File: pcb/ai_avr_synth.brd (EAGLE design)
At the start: 99.1 x 69.8 mm, 49 parts, among them IC1 ATMEGA328P-PDIP, J1 1X02ST, J2 1X06, J3 1X08, J4 1X08, J5 MIDIJACK, U1 MC7805, U2 TLC2262, U3 6N138

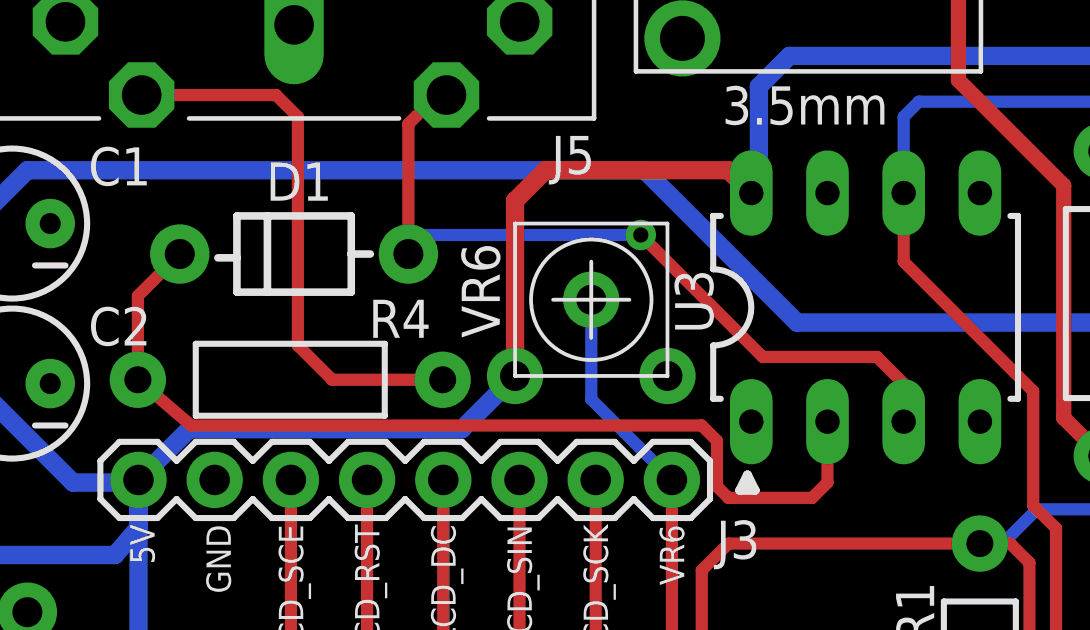
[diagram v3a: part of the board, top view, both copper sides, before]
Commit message: fixed trimmer footprint
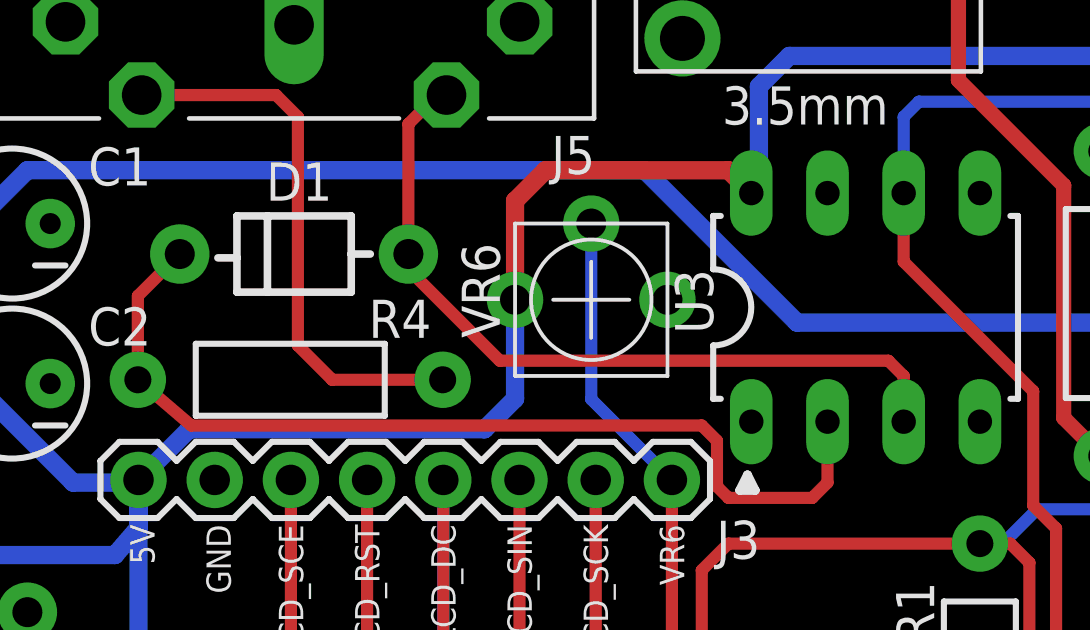
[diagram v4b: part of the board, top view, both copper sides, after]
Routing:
- net LCD_LED: track 47.1 -> 49.7 mm
- net N$10: track 26.1 -> 26.0 mm, vias 1 -> 0
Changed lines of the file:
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@@
 <wire x1="49.53" y1="57.404" x2="48.26" y2="56.134" width="0.6096" layer="1"/>
 <wire x1="13.61" y1="42" x2="15.298" y2="43.688" width="0.6096" layer="16"/>
-<wire x1="15.298" y1="43.688" x2="24.384" y2="43.688" width="0.6096" layer="16"/>
-<wire x1="24.384" y1="43.688" x2="26.162" y2="45.466" width="0.6096" layer="16"/>
-<wire x1="26.162" y1="45.466" x2="26.162" y2="51.308" width="0.6096" layer="1"/>
+<wire x1="15.298" y1="43.688" x2="25.146" y2="43.688" width="0.6096" layer="16"/>
+<wire x1="26.162" y1="48.006" x2="26.162" y2="51.308" width="0.6096" layer="1"/>
 <wire x1="26.162" y1="51.308" x2="27.178" y2="52.324" width="0.6096" layer="1"/>
 <wire x1="27.178" y1="52.324" x2="33.274" y2="52.324" width="0.6096" layer="1"/>
@@
 <wire x1="34.29" y1="55.118" x2="35.306" y2="56.134" width="0.6096" layer="16"/>
 <wire x1="35.306" y1="56.134" x2="48.26" y2="56.134" width="0.6096" layer="16"/>
+<wire x1="26.162" y1="48.006" x2="26.162" y2="44.704" width="0.6096" layer="16"/>
+<wire x1="26.162" y1="44.704" x2="25.146" y2="43.688" width="0.6096" layer="16"/>
 </signal>
 <signal name="RESET">
@@
 <wire x1="31.39" y1="2" x2="31.39" y2="42" width="0.4064" layer="1"/>
 <contactref element="VR6" pad="2"/>
-<wire x1="28.702" y1="48.006" x2="28.702" y2="44.688" width="0.4064" layer="16"/>
+<wire x1="28.702" y1="50.546" x2="28.702" y2="44.688" width="0.4064" layer="16"/>
 <wire x1="28.702" y1="44.688" x2="31.39" y2="42" width="0.4064" layer="16"/>
 </signal>
@@
 <contactref element="D1" pad="A"/>
 <contactref element="U3" pad="3"/>
-<wire x1="22.606" y1="49.53" x2="23.241" y2="50.165" width="0.4064" layer="16"/>
-<wire x1="23.241" y1="50.165" x2="30.353" y2="50.165" width="0.4064" layer="16"/>
-<via x="30.353" y="50.165" extent="1-16" drill="0.508"/>
-<wire x1="30.353" y1="50.165" x2="34.417" y2="46.101" width="0.4064" layer="1"/>
-<wire x1="34.417" y1="46.101" x2="38.227" y2="46.101" width="0.4064" layer="1"/>
-<wire x1="38.227" y1="46.101" x2="39.116" y2="45.212" width="0.4064" layer="1"/>
-<wire x1="39.116" y1="45.212" x2="39.116" y2="43.942" width="0.4064" layer="1"/>
 <wire x1="22.606" y1="49.53" x2="22.606" y2="53.866" width="0.4064" layer="1"/>
 <contactref element="J5" pad="5"/>
 <wire x1="23.876" y1="54.83" x2="23.57" y2="54.83" width="0.4064" layer="1"/>
 <wire x1="23.57" y1="54.83" x2="22.606" y2="53.866" width="0.4064" layer="1"/>
+<wire x1="22.606" y1="49.53" x2="22.606" y2="49.022" width="0.4064" layer="1"/>
+<wire x1="22.606" y1="49.022" x2="25.654" y2="45.974" width="0.4064" layer="1"/>
+<wire x1="25.654" y1="45.974" x2="38.608" y2="45.974" width="0.4064" layer="1"/>
+<wire x1="38.608" y1="45.974" x2="39.116" y2="45.466" width="0.4064" layer="1"/>
+<wire x1="39.116" y1="45.466" x2="39.116" y2="43.942" width="0.4064" layer="1"/>
 </signal>
 <signal name="N$12">

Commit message: updating
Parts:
- D1: value (none) -> 1N4148
- D2: value (none) -> 1N4001
- IC1: device Ai_IC:DIL28-3 -> Ai_IC:DIL28
- STANDOFF5, STANDOFF6, STANDOFF7, STANDOFF8: value STAND-OFF -> STAND-OFF4; device Ai_Electromechanical:STAND-OFF -> Ai_Electromechanical:STAND-OFF-4
- U$5: value AI-LOGOL -> AI-LOGOXS; device Ai_Miscellany:AI-LOGO-L -> Ai_Miscellany:AI-LOGO-XS
- U1: value MC7805 -> MC7805-HOR
- U2, U3: device Ai_IC:DIL08-3 -> Ai_IC:DIL08
- XL1: device Ai_FrequencyControl:CRYSTAL-HC49S -> Ai_FrequencyControl:HC49S
- moved VR6 2.50 mm to (28.1, 50.4), turned to 270 degrees
- moved VR1 1.50 mm to (52.3, 34.0)
- moved R4 1.14 mm to (18.7, 46.5)
- moved U$5 1.08 mm to (65.5, 61.3)
- moved S8 1.02 mm to (2.29, 50.9)
- moved J3 1.00 mm to (22.5, 43.0)
- moved J4 1.00 mm to (22.5, 3.00)
- moved VR2 1.00 mm to (65.8, 34.0)
- moved C1 0.80 mm to (9.14, 51.3)
- moved C2 0.80 mm to (9.14, 46.0)
- moved D1 0.76 mm to (18.8, 50.3)
- moved VR3 0.50 mm to (79.2, 34.0)
- moved J1 0.38 mm to (3.68, 60.5)
- renumbered J2 to FTDI
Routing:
- net 9V: track 66.1 -> 73.5 mm
- net 5V: track 269.9 -> 272.0 mm
- net N$10: track 26.0 -> 28.1 mm
- net LCD_LED: track 49.7 -> 47.7 mm
- net N$1: track 18.4 -> 17.3 mm
- net LCD_DC: track 116.5 -> 117.5 mm
- net TXO: track 59.7 -> 60.6 mm
- net N$9: track 32.5 -> 33.3 mm
- net SEMIS: track 21.7 -> 22.4 mm
- net LCD_SCK: track 77.9 -> 77.2 mm
- net CENTS: track 18.6 -> 18.0 mm
- net N$5: track 17.4 -> 16.8 mm
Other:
- outline, holes or cut-outs redrawn
- board text added: "ACROBOTIC Synth Kit"
- board text added: "http://acrobotic.com/synth-kit"
- board text added: "v1.3"
- board text removed: "Ai AVR SYNTHESIZER"
- board text removed: "Design by: Sam Stratter (humanHardDrive)"
- board text removed: "http://acrobotic.com/avr-synthesizer"
- board text removed: "v1.2"

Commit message: adding additional licensing information
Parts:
- added FRAME1: FRAME-LETTER, Ai_Miscellany:CREATIVE-COMMONS
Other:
- board text added: "@MakerBro"
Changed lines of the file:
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@@
 <?xml version="1.0" encoding="utf-8"?>
 <!DOCTYPE eagle SYSTEM "eagle.dtd">
-<eagle version="6.5.0">
+<eagle version="7.1.0">
 <drawing>
 <settings>
@@
 <setting verticaltext="up"/>
 </settings>
-<grid distance="5" unitdist="mil" unit="mil" style="lines" multiple="1" display="yes" altdistance="0.025" altunitdist="inch" altunit="inch"/>
+<grid distance="50" unitdist="mil" unit="mil" style="lines" multiple="1" display="yes" altdistance="0.025" altunitdist="inch" altunit="inch"/>
 <layers>
 <layer number="1" name="Top" color="4" fill="1" visible="yes" active="yes"/>
@@
 <layer number="20" name="Dimension" color="15" fill="1" visible="yes" active="yes"/>
 <layer number="21" name="tPlace" color="7" fill="1" visible="yes" active="yes"/>
-<layer number="22" name="bPlace" color="7" fill="1" visible="yes" active="yes"/>
+<layer number="22" name="bPlace" color="13" fill="1" visible="yes" active="yes"/>
 <layer number="23" name="tOrigins" color="15" fill="1" visible="yes" active="yes"/>
 <layer number="24" name="bOrigins" color="15" fill="1" visible="yes" active="yes"/>
@@
 <layer number="49" name="Reference" color="7" fill="1" visible="yes" active="yes"/>
 <layer number="50" name="dxf" color="7" fill="1" visible="no" active="no"/>
-<layer number="51" name="tDocu" color="7" fill="1" visible="no" active="yes"/>
+<layer number="51" name="tDocu" color="14" fill="1" visible="yes" active="yes"/>
 <layer number="52" name="bDocu" color="7" fill="1" visible="no" active="yes"/>
 <layer number="53" name="tGND_GNDA" color="7" fill="9" visible="no" active="no"/>
@@
 <layer number="59" name="tCarbon" color="7" fill="1" visible="no" active="no"/>
 <layer number="60" name="bCarbon" color="7" fill="1" visible="no" active="no"/>
-<layer number="90" name="Modules" color="5" fill="1" visible="yes" active="yes"/>
+<layer number="90" name="Modules" color="5" fill="1" visible="no" active="no"/>
 <layer number="91" name="Nets" color="2" fill="1" visible="no" active="no"/>
 <layer number="92" name="Busses" color="1" fill="1" visible="no" active="no"/>
@@
 <text x="30.861" y="41.529" size="0.8128" layer="21" font="vector" ratio="10" rot="R270">VR6</text>
 <text x="5.969" y="47.498" size="1.27" layer="21" font="vector" ratio="10" rot="R90">ON | OFF</text>
+<text x="45.72" y="-17.78" size="1.524" layer="51" font="vector" ratio="10">@MakerBro</text>
 </plain>
 <attributes>
@@
 <pass name="Default">
 <param name="RoutingGrid" value="50mil"/>
+<param name="AutoGrid" value="1"/>
+<param name="Efforts" value="0"/>
+<param name="TopRouterVariant" value="1"/>
 <param name="tpViaShape" value="round"/>
 <param name="PrefDir.1" value="|"/>
@@
 <attribute name="NAME" x="8.509" y="69.215" size="1.27" layer="25" font="vector" ratio="10" rot="R180"/>
 </element>
+<element name="FRAME1" library="Ai_Miscellany" package="CREATIVE-COMMONS" value="FRAME-LETTER" x="52.07" y="-1.27">
+<attribute name="REV" value="1.3" x="52.07" y="-1.27" size="1.524" layer="27" font="vector" ratio="10" display="off"/>
+</element>
 </elements>
 <signals>
@@
 </board>
 </drawing>
+<compatibility>
+<note version="6.3" minversion="6.2.2" severity="warning">
+Since Version 6.2.2 text objects can contain more than one line,
+which will not be processed correctly with this version.
+</note>
+</compatibility>
 </eagle>

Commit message: updating
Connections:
- net RXI renamed TXD
- net TXO renamed RXD
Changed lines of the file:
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@@
 <?xml version="1.0" encoding="utf-8"?>
 <!DOCTYPE eagle SYSTEM "eagle.dtd">
-<eagle version="7.1.0">
+<eagle version="6.5.0">
 <drawing>
 <settings>
@@
 <text x="6.096" y="64.135" size="1.778" layer="21" font="vector" ratio="10">+</text>
 <text x="58.674" y="63.373" size="0.8128" layer="21" font="vector" ratio="10" rot="R180">DTR</text>
-<text x="56.007" y="63.373" size="0.8128" layer="21" font="vector" ratio="10" rot="R180">TXD</text>
+<text x="56.007" y="63.373" size="0.8128" layer="21" font="vector" ratio="10" rot="R180">RXD</text>
 <text x="45.466" y="63.373" size="0.8128" layer="21" font="vector" ratio="10" rot="R180">GND</text>
 <text x="50.8" y="63.373" size="0.8128" layer="21" font="vector" ratio="10" rot="R180">VCC</text>
-<text x="53.467" y="63.373" size="0.8128" layer="21" font="vector" ratio="10" rot="R180">RXD</text>
+<text x="53.467" y="63.373" size="0.8128" layer="21" font="vector" ratio="10" rot="R180">TXD</text>
 <text x="65.532" y="66.04" size="0.889" layer="21" font="vector" ratio="10">http://acrobotic.com/synth-kit</text>
 <wire x1="47.498" y1="12.7" x2="47.752" y2="13.208" width="0.3048" layer="21"/>
@@
 <pass name="Default">
 <param name="RoutingGrid" value="50mil"/>
-<param name="AutoGrid" value="1"/>
-<param name="Efforts" value="0"/>
-<param name="TopRouterVariant" value="1"/>
 <param name="tpViaShape" value="round"/>
 <param name="PrefDir.1" value="|"/>
@@
 <wire x1="21.23" y1="43" x2="21.23" y2="3" width="0.4064" layer="1"/>
 </signal>
-<signal name="RXI">
+<signal name="TXD">
 <contactref element="IC1" pad="2"/>
 <contactref element="U3" pad="6"/>
@@
 <wire x1="52.07" y1="56.388" x2="52.07" y2="65.024" width="0.4064" layer="16"/>
 </signal>
-<signal name="TXO">
+<signal name="RXD">
 <contactref element="IC1" pad="3"/>
 <contactref element="FTDI" pad="5"/>
